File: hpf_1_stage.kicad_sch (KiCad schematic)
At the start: 5 parts, among them U2 TL072

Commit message: Re-annotate and run erc
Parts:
- renumbered C1 to C5, C2 to C6, R7 to R10, R8 to R11
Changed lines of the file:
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@@
   (symbol (lib_id "Device:C") (at 83.82 59.69 90) (unit 1)
     (in_bom yes) (on_board yes) (dnp no) (fields_autoplaced)
-    (property "Reference" "C2" (at 83.82 52.07 90)
+    (property "Reference" "C6" (at 83.82 52.07 90)
       (effects (font (size 1.27 1.27)))
     )
@@
       (project "crossover"
         (path "/3c8df2a5-e9f9-4495-af40-aa221f0b3fa5/3cc5a9b3-0b38-4f73-8059-4b4ed0453094/dae50590-4e4f-42fe-b7c9-e0e0ba94a145"
-          (reference "C2") (unit 1)
-        )
-        (path "/3c8df2a5-e9f9-4495-af40-aa221f0b3fa5/3cc5a9b3-0b38-4f73-8059-4b4ed0453094/b4ab64b4-4617-4eee-a838-7a71832e03e9"
-          (reference "C4") (unit 1)
-        )
-        (path "/3c8df2a5-e9f9-4495-af40-aa221f0b3fa5/965c39b4-975b-4eb7-b838-2ecc6e0d6a35/dae50590-4e4f-42fe-b7c9-e0e0ba94a145"
           (reference "C6") (unit 1)
         )
-        (path "/3c8df2a5-e9f9-4495-af40-aa221f0b3fa5/965c39b4-975b-4eb7-b838-2ecc6e0d6a35/b4ab64b4-4617-4eee-a838-7a71832e03e9"
+        (path "/3c8df2a5-e9f9-4495-af40-aa221f0b3fa5/3cc5a9b3-0b38-4f73-8059-4b4ed0453094/b4ab64b4-4617-4eee-a838-7a71832e03e9"
           (reference "C8") (unit 1)
+        )
+        (path "/3c8df2a5-e9f9-4495-af40-aa221f0b3fa5/965c39b4-975b-4eb7-b838-2ecc6e0d6a35/dae50590-4e4f-42fe-b7c9-e0e0ba94a145"
+          (reference "C10") (unit 1)
+        )
+        (path "/3c8df2a5-e9f9-4495-af40-aa221f0b3fa5/965c39b4-975b-4eb7-b838-2ecc6e0d6a35/b4ab64b4-4617-4eee-a838-7a71832e03e9"
+          (reference "C12") (unit 1)
         )
       )
@@
   (symbol (lib_id "Device:C") (at 68.58 59.69 90) (unit 1)
     (in_bom yes) (on_board yes) (dnp no) (fields_autoplaced)
-    (property "Reference" "C1" (at 68.58 52.07 90)
+    (property "Reference" "C5" (at 68.58 52.07 90)
       (effects (font (size 1.27 1.27)))
     )
@@
       (project "crossover"
         (path "/3c8df2a5-e9f9-4495-af40-aa221f0b3fa5/3cc5a9b3-0b38-4f73-8059-4b4ed0453094/dae50590-4e4f-42fe-b7c9-e0e0ba94a145"
-          (reference "C1") (unit 1)
-        )
-        (path "/3c8df2a5-e9f9-4495-af40-aa221f0b3fa5/3cc5a9b3-0b38-4f73-8059-4b4ed0453094/b4ab64b4-4617-4eee-a838-7a71832e03e9"
-          (reference "C3") (unit 1)
-        )
-        (path "/3c8df2a5-e9f9-4495-af40-aa221f0b3fa5/965c39b4-975b-4eb7-b838-2ecc6e0d6a35/dae50590-4e4f-42fe-b7c9-e0e0ba94a145"
           (reference "C5") (unit 1)
         )
-        (path "/3c8df2a5-e9f9-4495-af40-aa221f0b3fa5/965c39b4-975b-4eb7-b838-2ecc6e0d6a35/b4ab64b4-4617-4eee-a838-7a71832e03e9"
+        (path "/3c8df2a5-e9f9-4495-af40-aa221f0b3fa5/3cc5a9b3-0b38-4f73-8059-4b4ed0453094/b4ab64b4-4617-4eee-a838-7a71832e03e9"
           (reference "C7") (unit 1)
         )
+        (path "/3c8df2a5-e9f9-4495-af40-aa221f0b3fa5/965c39b4-975b-4eb7-b838-2ecc6e0d6a35/dae50590-4e4f-42fe-b7c9-e0e0ba94a145"
+          (reference "C9") (unit 1)
+        )
+        (path "/3c8df2a5-e9f9-4495-af40-aa221f0b3fa5/965c39b4-975b-4eb7-b838-2ecc6e0d6a35/b4ab64b4-4617-4eee-a838-7a71832e03e9"
+          (reference "C11") (unit 1)
+        )
       )
     )
@@
   (symbol (lib_id "power:GNDREF") (at 91.44 78.74 0) (unit 1)
     (in_bom yes) (on_board yes) (dnp no) (fields_autoplaced)
-    (property "Reference" "#PWR06" (at 91.44 85.09 0)
+    (property "Reference" "#PWR09" (at 91.44 85.09 0)
       (effects (font (size 1.27 1.27)) hide)
     )
@@
       (project "crossover"
         (path "/3c8df2a5-e9f9-4495-af40-aa221f0b3fa5/3cc5a9b3-0b38-4f73-8059-4b4ed0453094/dae50590-4e4f-42fe-b7c9-e0e0ba94a145"
-          (reference "#PWR06") (unit 1)
-        )
-        (path "/3c8df2a5-e9f9-4495-af40-aa221f0b3fa5/3cc5a9b3-0b38-4f73-8059-4b4ed0453094/b4ab64b4-4617-4eee-a838-7a71832e03e9"
-          (reference "#PWR07") (unit 1)
-        )
-        (path "/3c8df2a5-e9f9-4495-af40-aa221f0b3fa5/965c39b4-975b-4eb7-b838-2ecc6e0d6a35/dae50590-4e4f-42fe-b7c9-e0e0ba94a145"
-          (reference "#PWR08") (unit 1)
-        )
-        (path "/3c8df2a5-e9f9-4495-af40-aa221f0b3fa5/965c39b4-975b-4eb7-b838-2ecc6e0d6a35/b4ab64b4-4617-4eee-a838-7a71832e03e9"
           (reference "#PWR09") (unit 1)
         )
+        (path "/3c8df2a5-e9f9-4495-af40-aa221f0b3fa5/3cc5a9b3-0b38-4f73-8059-4b4ed0453094/b4ab64b4-4617-4eee-a838-7a71832e03e9"
+          (reference "#PWR010") (unit 1)
+        )
+        (path "/3c8df2a5-e9f9-4495-af40-aa221f0b3fa5/965c39b4-975b-4eb7-b838-2ecc6e0d6a35/dae50590-4e4f-42fe-b7c9-e0e0ba94a145"
+          (reference "#PWR011") (unit 1)
+        )
+        (path "/3c8df2a5-e9f9-4495-af40-aa221f0b3fa5/965c39b4-975b-4eb7-b838-2ecc6e0d6a35/b4ab64b4-4617-4eee-a838-7a71832e03e9"
+          (reference "#PWR012") (unit 1)
+        )
       )
     )
@@
   (symbol (lib_id "Device:R") (at 99.06 48.26 90) (unit 1)
     (in_bom yes) (on_board yes) (dnp no) (fields_autoplaced)
-    (property "Reference" "R8" (at 99.06 41.91 90)
+    (property "Reference" "R11" (at 99.06 41.91 90)
       (effects (font (size 1.27 1.27)))
     )
@@
       (project "crossover"
         (path "/3c8df2a5-e9f9-4495-af40-aa221f0b3fa5/3cc5a9b3-0b38-4f73-8059-4b4ed0453094/dae50590-4e4f-42fe-b7c9-e0e0ba94a145"
-          (reference "R8") (unit 1)
-        )
-        (path "/3c8df2a5-e9f9-4495-af40-aa221f0b3fa5/3cc5a9b3-0b38-4f73-8059-4b4ed0453094/b4ab64b4-4617-4eee-a838-7a71832e03e9"
-          (reference "R10") (unit 1)
-        )
-        (path "/3c8df2a5-e9f9-4495-af40-aa221f0b3fa5/965c39b4-975b-4eb7-b838-2ecc6e0d6a35/dae50590-4e4f-42fe-b7c9-e0e0ba94a145"
-          (reference "R12") (unit 1)
-        )
-        (path "/3c8df2a5-e9f9-4495-af40-aa221f0b3fa5/965c39b4-975b-4eb7-b838-2ecc6e0d6a35/b4ab64b4-4617-4eee-a838-7a71832e03e9"
-          (reference "R14") (unit 1)
+          (reference "R11") (unit 1)
+        )
+        (path "/3c8df2a5-e9f9-4495-af40-aa221f0b3fa5/3cc5a9b3-0b38-4f73-8059-4b4ed0453094/b4ab64b4-4617-4eee-a838-7a71832e03e9"
+          (reference "R13") (unit 1)
+        )
+        (path "/3c8df2a5-e9f9-4495-af40-aa221f0b3fa5/965c39b4-975b-4eb7-b838-2ecc6e0d6a35/dae50590-4e4f-42fe-b7c9-e0e0ba94a145"
+          (reference "R15") (unit 1)
+        )
+        (path "/3c8df2a5-e9f9-4495-af40-aa221f0b3fa5/965c39b4-975b-4eb7-b838-2ecc6e0d6a35/b4ab64b4-4617-4eee-a838-7a71832e03e9"
+          (reference "R17") (unit 1)
         )
       )
@@
   (symbol (lib_id "Device:R") (at 91.44 68.58 0) (unit 1)
     (in_bom yes) (on_board yes) (dnp no) (fields_autoplaced)
-    (property "Reference" "R7" (at 93.98 67.3099 0)
+    (property "Reference" "R10" (at 93.98 67.3099 0)
       (effects (font (size 1.27 1.27)) (justify left))
     )
@@
       (project "crossover"
         (path "/3c8df2a5-e9f9-4495-af40-aa221f0b3fa5/3cc5a9b3-0b38-4f73-8059-4b4ed0453094/dae50590-4e4f-42fe-b7c9-e0e0ba94a145"
-          (reference "R7") (unit 1)
-        )
-        (path "/3c8df2a5-e9f9-4495-af40-aa221f0b3fa5/3cc5a9b3-0b38-4f73-8059-4b4ed0453094/b4ab64b4-4617-4eee-a838-7a71832e03e9"
-          (reference "R9") (unit 1)
-        )
-        (path "/3c8df2a5-e9f9-4495-af40-aa221f0b3fa5/965c39b4-975b-4eb7-b838-2ecc6e0d6a35/dae50590-4e4f-42fe-b7c9-e0e0ba94a145"
-          (reference "R11") (unit 1)
-        )
-        (path "/3c8df2a5-e9f9-4495-af40-aa221f0b3fa5/965c39b4-975b-4eb7-b838-2ecc6e0d6a35/b4ab64b4-4617-4eee-a838-7a71832e03e9"
-          (reference "R13") (unit 1)
-        )
-      )
+          (reference "R10") (unit 1)
+        )
+        (path "/3c8df2a5-e9f9-4495-af40-aa221f0b3fa5/3cc5a9b3-0b38-4f73-8059-4b4ed0453094/b4ab64b4-4617-4eee-a838-7a71832e03e9"
+          (reference "R12") (unit 1)
+        )
+        (path "/3c8df2a5-e9f9-4495-af40-aa221f0b3fa5/965c39b4-975b-4eb7-b838-2ecc6e0d6a35/dae50590-4e4f-42fe-b7c9-e0e0ba94a145"
+          (reference "R14") (unit 1)
+        )
+        (path "/3c8df2a5-e9f9-4495-af40-aa221f0b3fa5/965c39b4-975b-4eb7-b838-2ecc6e0d6a35/b4ab64b4-4617-4eee-a838-7a71832e03e9"
+          (reference "R16") (unit 1)
+        )
+      )

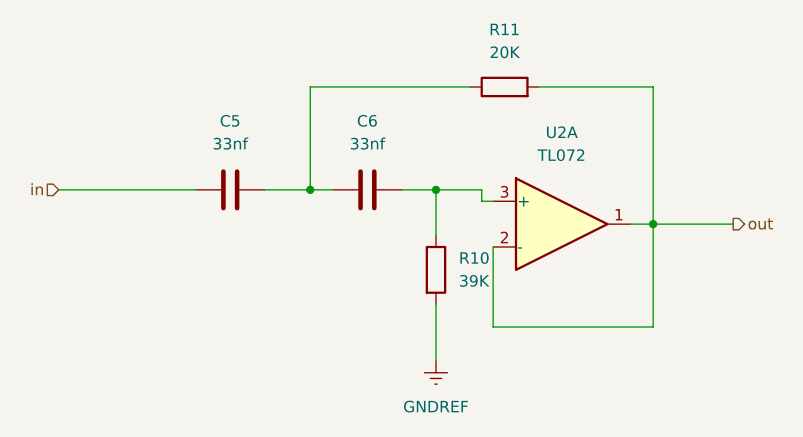
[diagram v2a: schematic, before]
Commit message: Switch to TL074
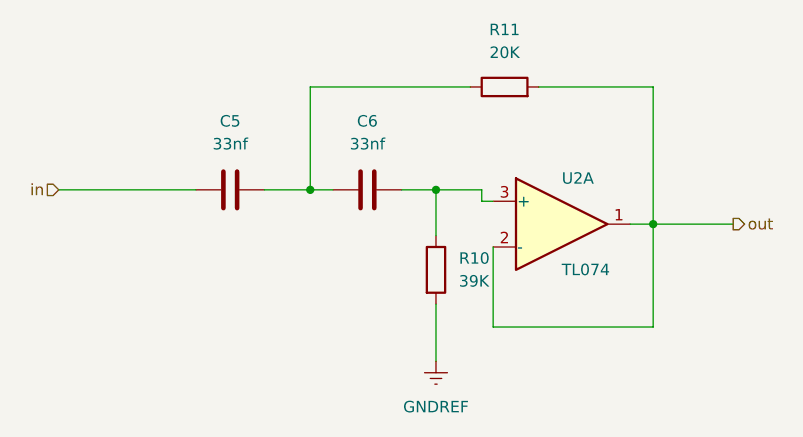
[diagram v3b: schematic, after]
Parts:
- U2: value TL072 -> TL074; footprint Package_DIP:DIP-8_W7.62mm_Socket -> (none); symbol Amplifier_Operational:TL072 -> Amplifier_Operational:TL074
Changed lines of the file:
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@@
     )
   )
-  (symbol (lib_id "Amplifier_Operational:TL072") (at 105.41 63.5 0) (unit 1)
+  (symbol (lib_id "Amplifier_Operational:TL074") (at 105.41 63.5 0) (unit 1)
     (in_bom yes) (on_board yes) (dnp no) (fields_autoplaced)
-    (property "Reference" "U2" (at 105.41 53.34 0)
-      (effects (font (size 1.27 1.27)))
+    (property "Reference" "U2" (at 105.41 58.42 0)
+      (effects (font (size 1.27 1.27)) (justify left))
     )
-    (property "Value" "TL072" (at 105.41 55.88 0)
-      (effects (font (size 1.27 1.27)))
+    (property "Value" "TL074" (at 105.41 68.58 0)
+      (effects (font (size 1.27 1.27)) (justify left))
     )
-    (property "Footprint" "Package_DIP:DIP-8_W7.62mm_Socket" (at 105.41 63.5 0)
+    (property "Footprint" "" (at 104.14 60.96 0)
       (effects (font (size 1.27 1.27)) hide)
     )
-    (property "Datasheet" "http://www.ti.com/lit/ds/symlink/tl071.pdf" (at 105.41 63.5 0)
+    (property "Datasheet" "http://www.ti.com/lit/ds/symlink/tl071.pdf" (at 106.68 58.42 0)
       (effects (font (size 1.27 1.27)) hide)
     )
@@
     (pin "6")
     (pin "7")
+    (pin "10")
+    (pin "8")
+    (pin "9")
+    (pin "12")
+    (pin "13")
+    (pin "14")
+    (pin "11")
     (pin "4")
-    (pin "8")
     (instances
       (project "crossover"

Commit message: Assign footprints to everything
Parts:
- R10, R11: footprint Resistor_THT:R_Axial_DIN0207_L6.3mm_D2.5mm_P7.62mm_Horizontal -> Resistor_SMD:R_1206_3216Metric_Pad1.30x1.75mm_HandSolder
- U2: footprint (none) -> Package_SO:SOIC-14-16_3.9x9.9mm_P1.27mm
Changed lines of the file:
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@@
       (effects (font (size 1.27 1.27)) (justify left))
     )
-    (property "Footprint" "" (at 104.14 60.96 0)
+    (property "Footprint" "Package_SO:SOIC-14-16_3.9x9.9mm_P1.27mm" (at 104.14 60.96 0)
       (effects (font (size 1.27 1.27)) hide)
     )
@@
       (effects (font (size 1.27 1.27)))
     )
-    (property "Footprint" "Resistor_THT:R_Axial_DIN0207_L6.3mm_D2.5mm_P7.62mm_Horizontal" (at 99.06 50.038 90)
+    (property "Footprint" "Resistor_SMD:R_1206_3216Metric_Pad1.30x1.75mm_HandSolder" (at 99.06 50.038 90)
       (effects (font (size 1.27 1.27)) hide)
     )
@@
       (effects (font (size 1.27 1.27)) (justify left))
     )
-    (property "Footprint" "Resistor_THT:R_Axial_DIN0207_L6.3mm_D2.5mm_P7.62mm_Horizontal" (at 89.662 68.58 90)
+    (property "Footprint" "Resistor_SMD:R_1206_3216Metric_Pad1.30x1.75mm_HandSolder" (at 89.662 68.58 90)
       (effects (font (size 1.27 1.27)) hide)
     )

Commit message: Finish placing
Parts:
- U2: footprint Package_SO:SOIC-14-16_3.9x9.9mm_P1.27mm -> Package_SO:SOIC-14_3.9x8.7mm_P1.27mm
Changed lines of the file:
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@@
       (effects (font (size 1.27 1.27)) (justify left))
     )
-    (property "Footprint" "Package_SO:SOIC-14-16_3.9x9.9mm_P1.27mm" (at 104.14 60.96 0)
+    (property "Footprint" "Package_SO:SOIC-14_3.9x8.7mm_P1.27mm" (at 104.14 60.96 0)
       (effects (font (size 1.27 1.27)) hide)
     )
